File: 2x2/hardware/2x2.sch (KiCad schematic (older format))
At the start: 9 parts

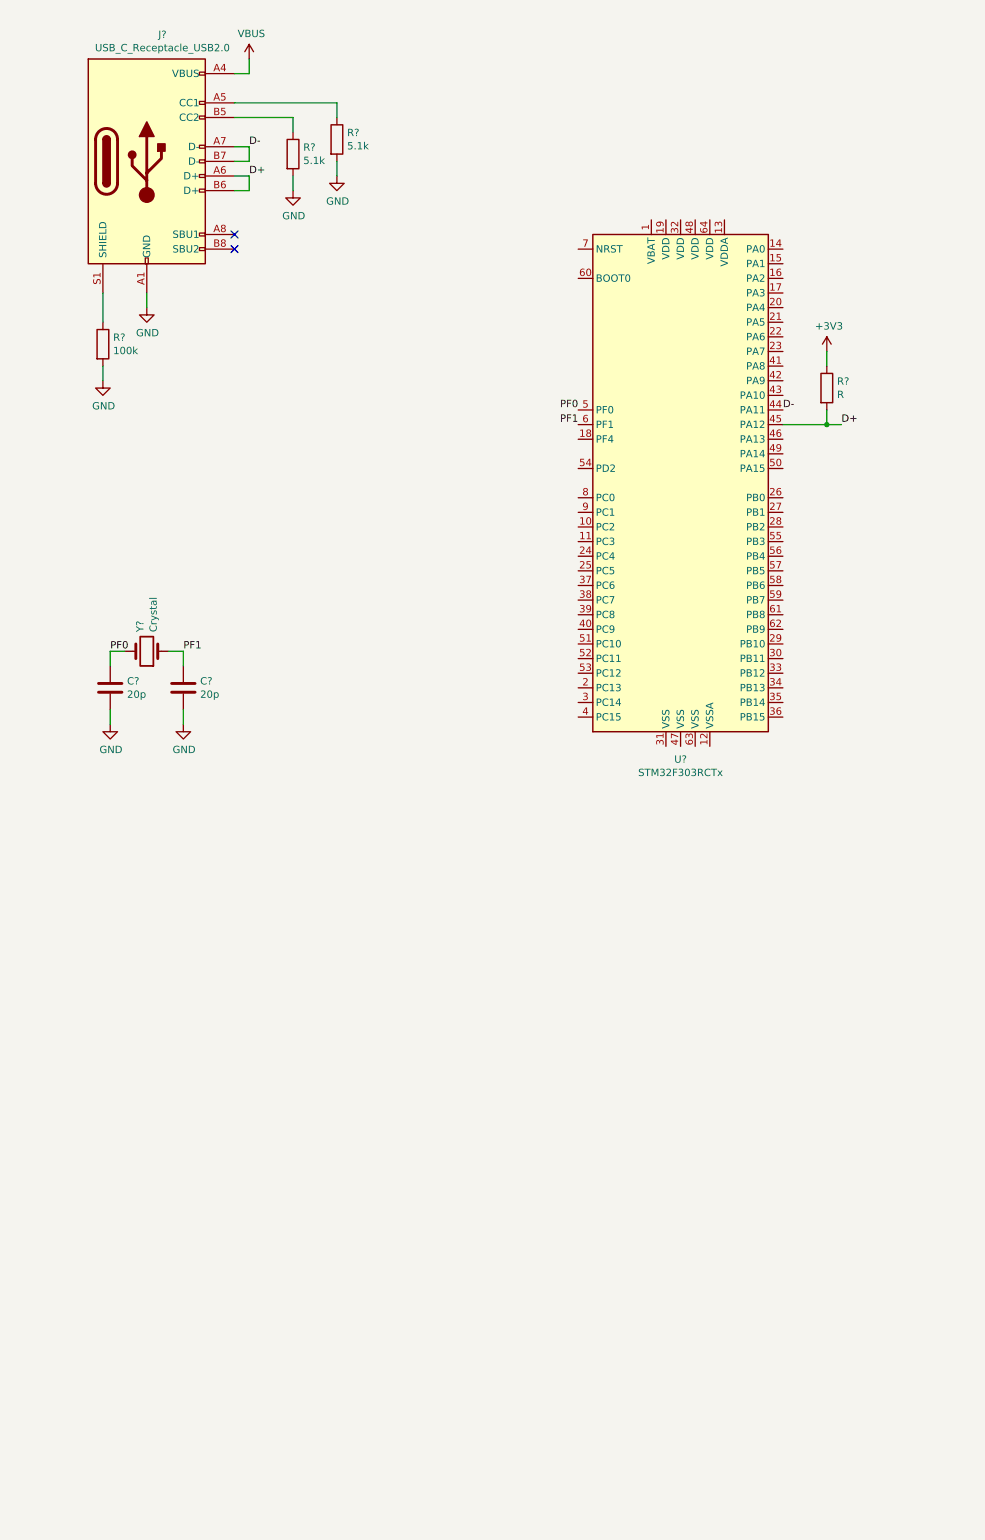
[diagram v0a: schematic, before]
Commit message: Add power protection diodes
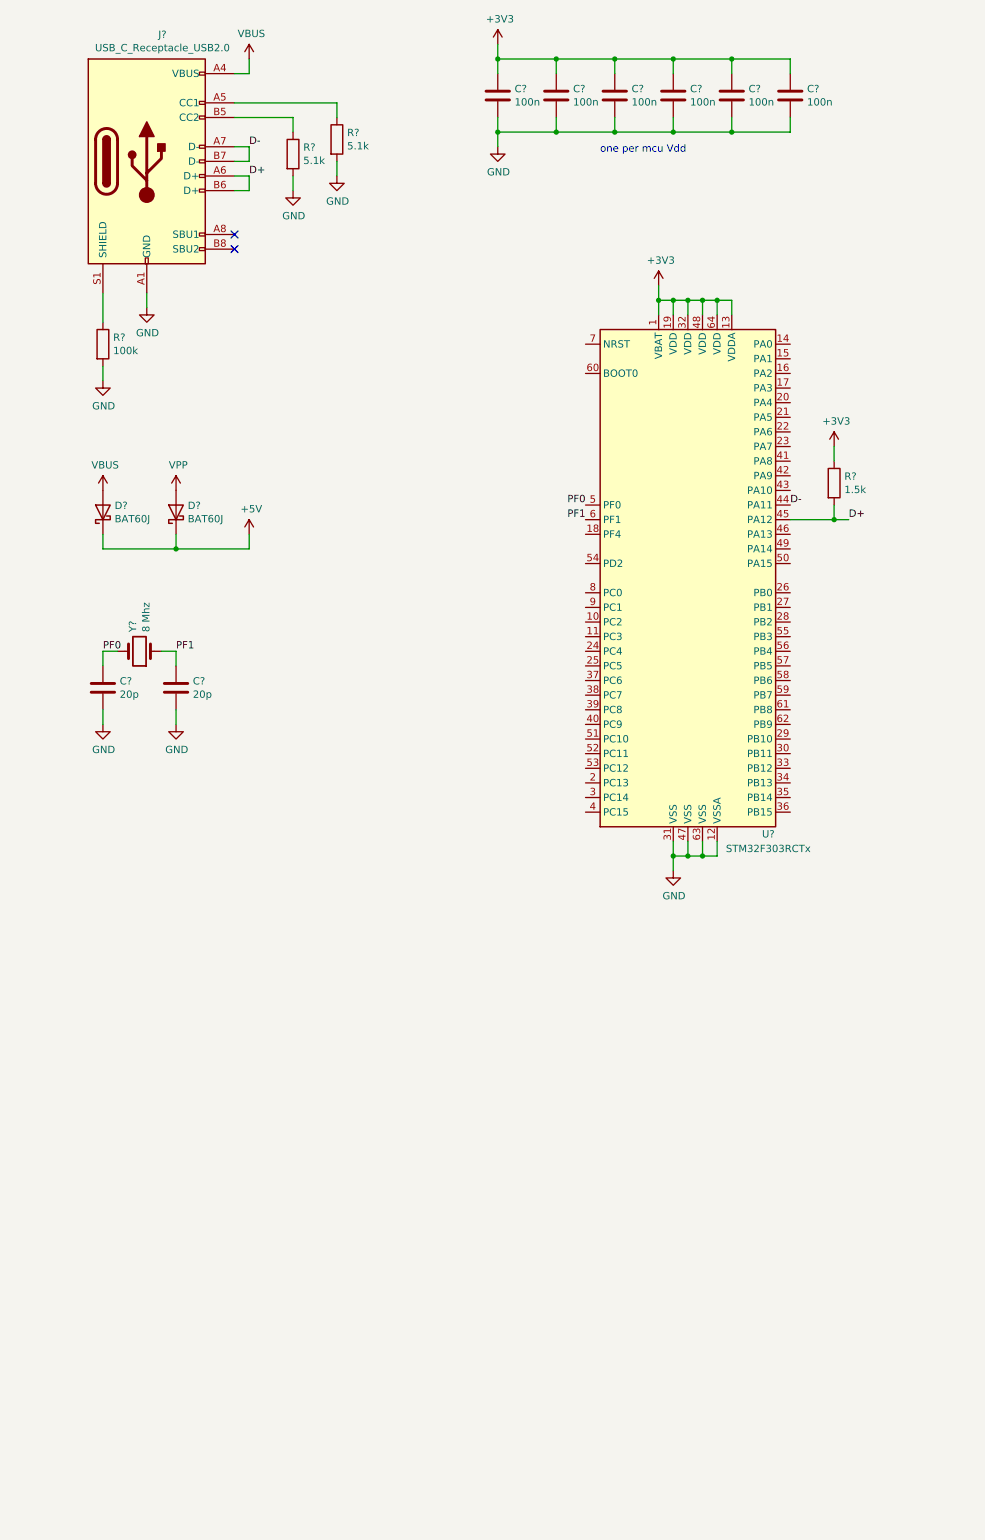
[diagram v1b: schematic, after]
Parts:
- added C? (x6): 100n, symbol Device:C
- added D? (x2): BAT60J, Diode_SMD:D_SOD-323, symbol User_Diode:BAT60J
- R?: value R -> 1.5k
- Y?: value Crystal -> 8 Mhz
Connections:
- net +3V3: now also U?.1 (VBAT), U?.13 (VDDA), U?.19 (VDD), U?.32 (VDD), U?.48 (VDD), U?.64 (VDD), C?.1, C?.1, C?.1, C?.1, C?.1, C?.1
- net GND: now also U?.12 (VSSA), U?.31 (VSS), U?.47 (VSS), U?.63 (VSS), C?.2, C?.2, C?.2, C?.2, C?.2, C?.2
- net VBUS: now also D?.2 (A)
- new net +5V: D?.1 (K), D?.1 (K)
- new net VPP: D?.2 (A)
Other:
- note added: "one per mcu Vdd"
- moved on the sheet: C?, R?, U?, Y?

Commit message: Add programming header to schematic
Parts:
- added J?: Conn_01x04, symbol Connector_Generic:Conn_01x04
- added R? (x2): R, symbol Device:R
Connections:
- net +3V3: now also R?.1
- net GND: now also J?.1 (Pin_1), R?.2
- net SWDIO: now reaches U?.46 (PA13)
- net SWDIO: now also J?.2 (Pin_2)
- net SWCLK: now reaches U?.49 (PA14)
- net SWCLK: now also J?.3 (Pin_3)
- net at U?.60 (BOOT0): now also R?.1
- net NRST: now reaches U?.7 (NRST)
- net NRST: now also J?.4 (Pin_4), R?.2
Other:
- moved on the sheet: R?
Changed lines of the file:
@@
 EELAYER 30 0
 EELAYER END
-$Descr A4 11693 8268
+$Descr A3 16535 11693
 encoding utf-8
 Sheet 1 1
@@
 	1    0    0    -1
 $EndComp
-Wire Wire Line
-	2100 1750 2200 1750
-Wire Wire Line
-	2200 1750 2200 1650
-Wire Wire Line
-	2200 1650 2100 1650
-Wire Wire Line
-	2100 1850 2200 1850
-Wire Wire Line
-	2200 1850 2200 1950
-Wire Wire Line
-	2200 1950 2100 1950
 $Comp
 L power:GND #PWR?
@@
 NoConn ~ 2100 2250
 NoConn ~ 2100 2350
-Text Label 2200 1650 0    50   ~ 0
+Text Label 2100 1650 0    50   ~ 0
 D-
-Text Label 2200 1850 0    50   ~ 0
+Text Label 2100 1850 0    50   ~ 0
 D+
 $Comp
@@
 $EndComp
 Wire Wire Line
-	2800 1750 2800 1850
-Wire Wire Line
-	2500 1850 2500 1950
-Wire Wire Line
-	2800 1350 2100 1350
-Wire Wire Line
-	2800 1450 2800 1350
-Wire Wire Line
-	2500 1450 2500 1550
-Wire Wire Line
-	2100 1450 2500 1450
+	2650 1750 2650 1850
+Wire Wire Line
+	2350 1850 2350 1950
+Wire Wire Line
+	2650 1450 2650 1350
+Wire Wire Line
+	2350 1450 2350 1550
 $Comp
 L Device:R R?
 U 1 1 5E18AD1E
-P 2800 1600
-F 0 "R?" H 2870 1646 50  0000 L CNN
-F 1 "5.1k" H 2870 1555 50  0000 L CNN
-F 2 "" V 2730 1600 50  0001 C CNN
-F 3 "~" H 2800 1600 50  0001 C CNN
-	1    2800 1600
+P 2650 1600
+F 0 "R?" H 2720 1646 50  0000 L CNN
+F 1 "5.1k" H 2720 1555 50  0000 L CNN
+F 2 "" V 2580 1600 50  0001 C CNN
+F 3 "~" H 2650 1600 50  0001 C CNN
+	1    2650 1600
 	1    0    0    -1
 $EndComp
@@
 L Device:R R?
 U 1 1 5E189B0B
-P 2500 1700
-F 0 "R?" H 2570 1746 50  0000 L CNN
-F 1 "5.1k" H 2570 1655 50  0000 L CNN
-F 2 "" V 2430 1700 50  0001 C CNN
-F 3 "~" H 2500 1700 50  0001 C CNN
-	1    2500 1700
+P 2350 1700
+F 0 "R?" H 2420 1746 50  0000 L CNN
+F 1 "5.1k" H 2420 1655 50  0000 L CNN
+F 2 "" V 2280 1700 50  0001 C CNN
+F 3 "~" H 2350 1700 50  0001 C CNN
+	1    2350 1700
 	1    0    0    -1
 $EndComp
@@
 L power:GND #PWR?
 U 1 1 5E189915
-P 2800 1850
-F 0 "#PWR?" H 2800 1600 50  0001 C CNN
-F 1 "GND" H 2805 1677 50  0000 C CNN
-F 2 "" H 2800 1850 50  0001 C CNN
-F 3 "" H 2800 1850 50  0001 C CNN
-	1    2800 1850
+P 2650 1850
+F 0 "#PWR?" H 2650 1600 50  0001 C CNN
+F 1 "GND" H 2655 1677 50  0000 C CNN
+F 2 "" H 2650 1850 50  0001 C CNN
+F 3 "" H 2650 1850 50  0001 C CNN
+	1    2650 1850
 	1    0    0    -1
 $EndComp
@@
 L power:GND #PWR?
 U 1 1 5E188C76
-P 2500 1950
-F 0 "#PWR?" H 2500 1700 50  0001 C CNN
-F 1 "GND" H 2505 1777 50  0000 C CNN
-F 2 "" H 2500 1950 50  0001 C CNN
-F 3 "" H 2500 1950 50  0001 C CNN
-	1    2500 1950
+P 2350 1950
+F 0 "#PWR?" H 2350 1700 50  0001 C CNN
+F 1 "GND" H 2355 1777 50  0000 C CNN
+F 2 "" H 2350 1950 50  0001 C CNN
+F 3 "" H 2350 1950 50  0001 C CNN
+	1    2350 1950
 	1    0    0    -1
 $EndComp
@@
 Text Notes 4600 1700 0    50   ~ 0
 one per mcu Vdd
+Text Label 2100 1750 0    50   ~ 0
+D-
+Text Label 2100 1950 0    50   ~ 0
+D+
+Wire Wire Line
+	2100 1450 2350 1450
+Wire Wire Line
+	2100 1350 2650 1350
+$Comp
+L power:GND #PWR?
+U 1 1 5E23C562
+P 6950 1550
+F 0 "#PWR?" H 6950 1300 50  0001 C CNN
+F 1 "GND" H 6955 1377 50  0000 C CNN
+F 2 "" H 6950 1550 50  0001 C CNN
+F 3 "" H 6950 1550 50  0001 C CNN
+	1    6950 1550
+	1    0    0    -1
+$EndComp
+Wire Wire Line
+	6950 1550 6950 1450
+Wire Wire Line
+	6950 1450 6850 1450
+$Comp
+L Connector_Generic:Conn_01x04 J?
+U 1 1 5E23F52F
+P 6650 1350
+F 0 "J?" H 6568 925 50  0000 C CNN
+F 1 "Conn_01x04" H 6568 1016 50  0000 C CNN
+F 2 "" H 6650 1350 50  0001 C CNN
+F 3 "~" H 6650 1350 50  0001 C CNN
+	1    6650 1350
+	-1   0    0    1
+$EndComp
+Text Label 6850 1350 0    50   ~ 0
+SWDIO
+Text Label 6850 1250 0    50   ~ 0
+SWCLK
+Text Label 6850 1150 0    50   ~ 0
+NRST
+Text Label 4300 3000 2    50   ~ 0
+NRST
+Text Label 5900 4400 0    50   ~ 0
+SWCLK
+Text Label 5900 4300 0    50   ~ 0
+SWDIO
+$Comp
+L power:GND #PWR?
+U 1 1 5E241E03
+P 4400 3700
+F 0 "#PWR?" H 4400 3450 50  0001 C CNN
+F 1 "GND" H 4405 3527 50  0000 C CNN
+F 2 "" H 4400 3700 50  0001 C CNN
+F 3 "" H 4400 3700 50  0001 C CNN
+	1    4400 3700
+	1    0    0    -1
+$EndComp
+$Comp
+L Device:R R?
+U 1 1 5E24232B
+P 4400 3450
+F 0 "R?" H 4470 3496 50  0000 L CNN
+F 1 "R" H 4470 3405 50  0000 L CNN
+F 2 "" V 4330 3450 50  0001 C CNN
+F 3 "~" H 4400 3450 50  0001 C CNN
+	1    4400 3450
+	1    0    0    -1
+$EndComp
+Wire Wire Line
+	4400 3300 4400 3200
+Wire Wire Line
+	4400 3200 4500 3200
+Wire Wire Line
+	4400 3600 4400 3700
+$Comp
+L Device:R R?
+U 1 1 5E24A0FC
+P 4400 2750
+F 0 "R?" H 4470 2796 50  0000 L CNN
+F 1 "R" H 4470 2705 50  0000 L CNN
+F 2 "" V 4330 2750 50  0001 C CNN
+F 3 "~" H 4400 2750 50  0001 C CNN
+	1    4400 2750
+	1    0    0    -1
+$EndComp
+$Comp
+L power:+3V3 #PWR?
+U 1 1 5E24A34D
+P 4400 2500
+F 0 "#PWR?" H 4400 2350 50  0001 C CNN
+F 1 "+3V3" H 4415 2673 50  0000 C CNN
+F 2 "" H 4400 2500 50  0001 C CNN
+F 3 "" H 4400 2500 50  0001 C CNN
+	1    4400 2500
+	1    0    0    -1
+$EndComp
+Wire Wire Line
+	4300 3000 4400 3000
+Wire Wire Line
+	4400 2900 4400 3000
+Connection ~ 4400 3000
+Wire Wire Line
+	4400 3000 4500 3000
+Wire Wire Line
+	4400 2600 4400 2500
 $EndSCHEMATC

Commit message: Add LDO regulator
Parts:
- removed D? (x2): BAT60J, Diode_SMD:D_SOD-323, symbol User_Diode:BAT60J
- removed R?: 100k, symbol Device:R
- added C? (x2): 10u, symbol Device:C
- added U?: AMS1117-3.3, Package_TO_SOT_SMD:SOT-223-3_TabPin2, symbol Regulator_Linear:AMS1117-3.3
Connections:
- net +3V3: now also C?.1, U?.2 (VO)
- net GND: now also J?.S1 (SHIELD), C?.1, C?.2, U?.1 (GND)
- net VBUS: now also C?.2, U?.3 (VI)
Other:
- moved on the sheet: C?, Y?
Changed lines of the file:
@@
 L Device:Crystal Y?
 U 1 1 5E17BF4D
-P 1450 5100
-F 0 "Y?" V 1496 4969 50  0000 R CNN
-F 1 "8 Mhz" V 1405 4969 50  0000 R CNN
-F 2 "" H 1450 5100 50  0001 C CNN
-F 3 "~" H 1450 5100 50  0001 C CNN
-	1    1450 5100
+P 3350 3450
+F 0 "Y?" V 3396 3319 50  0000 R CNN
+F 1 "8 Mhz" V 3305 3319 50  0000 R CNN
+F 2 "" H 3350 3450 50  0001 C CNN
+F 3 "~" H 3350 3450 50  0001 C CNN
+	1    3350 3450
 	-1   0    0    1
 $EndComp
@@
 L power:GND #PWR?
 U 1 1 5E17E420
-P 1200 5600
-F 0 "#PWR?" H 1200 5350 50  0001 C CNN
-F 1 "GND" H 1205 5427 50  0000 C CNN
-F 2 "" H 1200 5600 50  0001 C CNN
-F 3 "" H 1200 5600 50  0001 C CNN
-	1    1200 5600
+P 3100 3950
+F 0 "#PWR?" H 3100 3700 50  0001 C CNN
+F 1 "GND" H 3105 3777 50  0000 C CNN
+F 2 "" H 3100 3950 50  0001 C CNN
+F 3 "" H 3100 3950 50  0001 C CNN
+	1    3100 3950
 	1    0    0    -1
 $EndComp
@@
 L power:GND #PWR?
 U 1 1 5E17EA25
-P 1700 5600
-F 0 "#PWR?" H 1700 5350 50  0001 C CNN
-F 1 "GND" H 1705 5427 50  0000 C CNN
-F 2 "" H 1700 5600 50  0001 C CNN
-F 3 "" H 1700 5600 50  0001 C CNN
-	1    1700 5600
+P 3600 3950
+F 0 "#PWR?" H 3600 3700 50  0001 C CNN
+F 1 "GND" H 3605 3777 50  0000 C CNN
+F 2 "" H 3600 3950 50  0001 C CNN
+F 3 "" H 3600 3950 50  0001 C CNN
+	1    3600 3950
 	1    0    0    -1
 $EndComp
@@
 L Device:C C?
 U 1 1 5E17ED6C
-P 1700 5350
-F 0 "C?" H 1815 5396 50  0000 L CNN
-F 1 "20p" H 1815 5305 50  0000 L CNN
-F 2 "" H 1738 5200 50  0001 C CNN
-F 3 "~" H 1700 5350 50  0001 C CNN
-	1    1700 5350
+P 3600 3700
+F 0 "C?" H 3715 3746 50  0000 L CNN
+F 1 "20p" H 3715 3655 50  0000 L CNN
+F 2 "" H 3638 3550 50  0001 C CNN
+F 3 "~" H 3600 3700 50  0001 C CNN
+	1    3600 3700
 	1    0    0    -1
 $EndComp
@@
 L Device:C C?
 U 1 1 5E17F3FF
-P 1200 5350
-F 0 "C?" H 1315 5396 50  0000 L CNN
-F 1 "20p" H 1315 5305 50  0000 L CNN
-F 2 "" H 1238 5200 50  0001 C CNN
-F 3 "~" H 1200 5350 50  0001 C CNN
-	1    1200 5350
-	1    0    0    -1
-$EndComp
-Wire Wire Line
-	1300 5100 1200 5100
-Wire Wire Line
-	1200 5100 1200 5200
-Wire Wire Line
-	1200 5500 1200 5600
-Wire Wire Line
-	1700 5500 1700 5600
-Wire Wire Line
-	1700 5200 1700 5100
-Wire Wire Line
-	1700 5100 1600 5100
-Text Label 1200 5100 0    50   ~ 0
+P 3100 3700
+F 0 "C?" H 3215 3746 50  0000 L CNN
+F 1 "20p" H 3215 3655 50  0000 L CNN
+F 2 "" H 3138 3550 50  0001 C CNN
+F 3 "~" H 3100 3700 50  0001 C CNN
+	1    3100 3700
+	1    0    0    -1
+$EndComp
+Wire Wire Line
+	3200 3450 3100 3450
+Wire Wire Line
+	3100 3450 3100 3550
+Wire Wire Line
+	3100 3850 3100 3950
+Wire Wire Line
+	3600 3850 3600 3950
+Wire Wire Line
+	3600 3550 3600 3450
+Wire Wire Line
+	3600 3450 3500 3450
+Text Label 3100 3450 0    50   ~ 0
 PF0
-Text Label 1700 5100 0    50   ~ 0
+Text Label 3600 3450 0    50   ~ 0
 PF1
 Text Label 4500 4100 2    50   ~ 0
@@
 L power:GND #PWR?
 U 1 1 5E185BEA
-P 1500 2750
-F 0 "#PWR?" H 1500 2500 50  0001 C CNN
-F 1 "GND" H 1505 2577 50  0000 C CNN
-F 2 "" H 1500 2750 50  0001 C CNN
-F 3 "" H 1500 2750 50  0001 C CNN
-	1    1500 2750
+P 1500 2850
+F 0 "#PWR?" H 1500 2600 50  0001 C CNN
+F 1 "GND" H 1505 2677 50  0000 C CNN
+F 2 "" H 1500 2850 50  0001 C CNN
+F 3 "" H 1500 2850 50  0001 C CNN
+	1    1500 2850
 	1    0    0    -1
 $EndComp
@@
 Wire Wire Line
 	2200 1150 2100 1150
-Wire Wire Line
-	1500 2650 1500 2750
-$Comp
-L Device:R R?
-U 1 1 5E1941D3
-P 1200 3000
-F 0 "R?" H 1270 3046 50  0000 L CNN
-F 1 "100k" H 1270 2955 50  0000 L CNN
-F 2 "" V 1130 3000 50  0001 C CNN
-F 3 "~" H 1200 3000 50  0001 C CNN
-	1    1200 3000
-	1    0    0    -1
-$EndComp
-$Comp
-L power:GND #PWR?
-U 1 1 5E194D95
-P 1200 3250
-F 0 "#PWR?" H 1200 3000 50  0001 C CNN
-F 1 "GND" H 1205 3077 50  0000 C CNN
-F 2 "" H 1200 3250 50  0001 C CNN
-F 3 "" H 1200 3250 50  0001 C CNN
-	1    1200 3250
-	1    0    0    -1
-$EndComp
-Wire Wire Line
-	1200 3150 1200 3250
-Wire Wire Line
-	1200 2650 1200 2850
 Text Label 6300 4200 0    50   ~ 0
 D+
@@
 Wire Wire Line
 	5500 1550 5100 1550
-$Comp
-L power:VBUS #PWR?
-U 1 1 5E1CF111
-P 1200 4000
-F 0 "#PWR?" H 1200 3850 50  0001 C CNN
-F 1 "VBUS" H 1215 4173 50  0000 C CNN
-F 2 "" H 1200 4000 50  0001 C CNN
-F 3 "" H 1200 4000 50  0001 C CNN
-	1    1200 4000
-	1    0    0    -1
-$EndComp
-$Comp
-L power:VPP #PWR?
-U 1 1 5E1CF894
-P 1700 4000
-F 0 "#PWR?" H 1700 3850 50  0001 C CNN
-F 1 "VPP" H 1715 4173 50  0000 C CNN
-F 2 "" H 1700 4000 50  0001 C CNN
-F 3 "" H 1700 4000 50  0001 C CNN
-	1    1700 4000
-	1    0    0    -1
-$EndComp
-$Comp
-L User_Diode:BAT60J D?
-U 1 1 5E1DA3FD
-P 1200 4150
-F 0 "D?" V 1246 4070 50  0000 R CNN
-F 1 "BAT60J" V 1155 4070 50  0000 R CNN
-F 2 "Diode_SMD:D_SOD-323" H 1200 3975 50  0001 C CNN
-F 3 "https://www.st.com/resource/en/datasheet/bat60.pdf" H 1200 4150 50  0001 C CNN
-	1    1200 4150
-	0    -1   -1   0
-$EndComp
-$Comp
-L User_Diode:BAT60J D?
-U 1 1 5E1DB618
-P 1700 4150
-F 0 "D?" V 1746 4070 50  0000 R CNN
-F 1 "BAT60J" V 1655 4070 50  0000 R CNN
-F 2 "Diode_SMD:D_SOD-323" H 1700 3975 50  0001 C CNN
-F 3 "https://www.st.com/resource/en/datasheet/bat60.pdf" H 1700 4150 50  0001 C CNN
-	1    1700 4150
-	0    -1   -1   0
-$EndComp
-$Comp
-L power:+5V #PWR?
-U 1 1 5E1DECFA
-P 2200 4300
-F 0 "#PWR?" H 2200 4150 50  0001 C CNN
-F 1 "+5V" H 2215 4473 50  0000 C CNN
-F 2 "" H 2200 4300 50  0001 C CNN
-F 3 "" H 2200 4300 50  0001 C CNN
-	1    2200 4300
-	1    0    0    -1
-$EndComp
-Wire Wire Line
-	1200 4300 1200 4400
-Wire Wire Line
-	1200 4400 1700 4400
-Wire Wire Line
-	2200 4400 2200 4300
-Wire Wire Line
-	1700 4300 1700 4400
-Connection ~ 1700 4400
-Wire Wire Line
-	1700 4400 2200 4400
 Text Notes 4600 1700 0    50   ~ 0
 one per mcu Vdd
@@
 Wire Wire Line
 	4400 2600 4400 2500
+Wire Wire Line
+	1500 2650 1500 2750
+Wire Wire Line
+	1200 2650 1200 2750
+Wire Wire Line
+	1200 2750 1500 2750
+Connection ~ 1500 2750
+Wire Wire Line
+	1500 2750 1500 2850
+$Comp
+L Regulator_Linear:AMS1117-3.3 U?
+U 1 1 5E25DF5D
+P 1950 5350
+F 0 "U?" H 1950 5592 50  0000 C CNN
+F 1 "AMS1117-3.3" H 1950 5501 50  0000 C CNN
+F 2 "Package_TO_SOT_SMD:SOT-223-3_TabPin2" H 1950 5550 50  0001 C CNN
+F 3 "http://www.advanced-monolithic.com/pdf/ds1117.pdf" H 2050 5100 50  0001 C CNN
+	1    1950 5350
+	1    0    0    -1
+$EndComp
+$Comp
+L power:GND #PWR?
+U 1 1 5E271B38
+P 1950 5850
+F 0 "#PWR?" H 1950 5600 50  0001 C CNN
+F 1 "GND" H 1955 5677 50  0000 C CNN
+F 2 "" H 1950 5850 50  0001 C CNN
+F 3 "" H 1950 5850 50  0001 C CNN
+	1    1950 5850
+	1    0    0    -1
+$EndComp
+$Comp
+L power:VBUS #PWR?
+U 1 1 5E272465
+P 1450 5250
+F 0 "#PWR?" H 1450 5100 50  0001 C CNN
+F 1 "VBUS" H 1465 5423 50  0000 C CNN
+F 2 "" H 1450 5250 50  0001 C CNN
+F 3 "" H 1450 5250 50  0001 C CNN
+	1    1450 5250
+	1    0    0    -1
+$EndComp
+$Comp
+L power:+3V3 #PWR?
+U 1 1 5E2729E2
+P 2450 5250
+F 0 "#PWR?" H 2450 5100 50  0001 C CNN
+F 1 "+3V3" H 2465 5423 50  0000 C CNN
+F 2 "" H 2450 5250 50  0001 C CNN
+F 3 "" H 2450 5250 50  0001 C CNN
+	1    2450 5250
+	1    0    0    -1
+$EndComp
+$Comp
+L Device:C C?
+U 1 1 5E279D7D
+P 1700 5750
+F 0 "C?" V 1448 5750 50  0000 C CNN
+F 1 "10u" V 1539 5750 50  0000 C CNN
+F 2 "" H 1738 5600 50  0001 C CNN
+F 3 "~" H 1700 5750 50  0001 C CNN
+	1    1700 5750
+	0    1    1    0
+$EndComp
+$Comp
+L Device:C C?
+U 1 1 5E27AF32
+P 2200 5750
+F 0 "C?" V 1948 5750 50  0000 C CNN
+F 1 "10u" V 2039 5750 50  0000 C CNN
+F 2 "" H 2238 5600 50  0001 C CNN
+F 3 "~" H 2200 5750 50  0001 C CNN
+	1    2200 5750
+	0    1    1    0
+$EndComp
+Wire Wire Line
+	2450 5250 2450 5350
+Wire Wire Line
+	2450 5350 2250 5350
+Wire Wire Line
+	2350 5750 2450 5750
+Wire Wire Line
+	2450 5750 2450 5350
+Connection ~ 2450 5350
+Wire Wire Line
+	1950 5650 1950 5750
+Wire Wire Line
+	2050 5750 1950 5750
+Connection ~ 1950 5750
+Wire Wire Line
+	1950 5750 1950 5850
+Wire Wire Line
+	1850 5750 1950 5750
+Wire Wire Line
+	1550 5750 1450 5750
+Wire Wire Line
+	1450 5750 1450 5350
+Wire Wire Line
+	1650 5350 1450 5350
+Connection ~ 1450 5350
+Wire Wire Line
+	1450 5350 1450 5250
 $EndSCHEMATC
